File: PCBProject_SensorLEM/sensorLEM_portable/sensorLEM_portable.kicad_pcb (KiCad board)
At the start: 2 copper layers, 82 parts, among them CN1 DB2EVC-3.81-4P-GN, U1 VRB1212S-6WR3, U2 VRB1212S-6WR3, U3 FT-AX1D

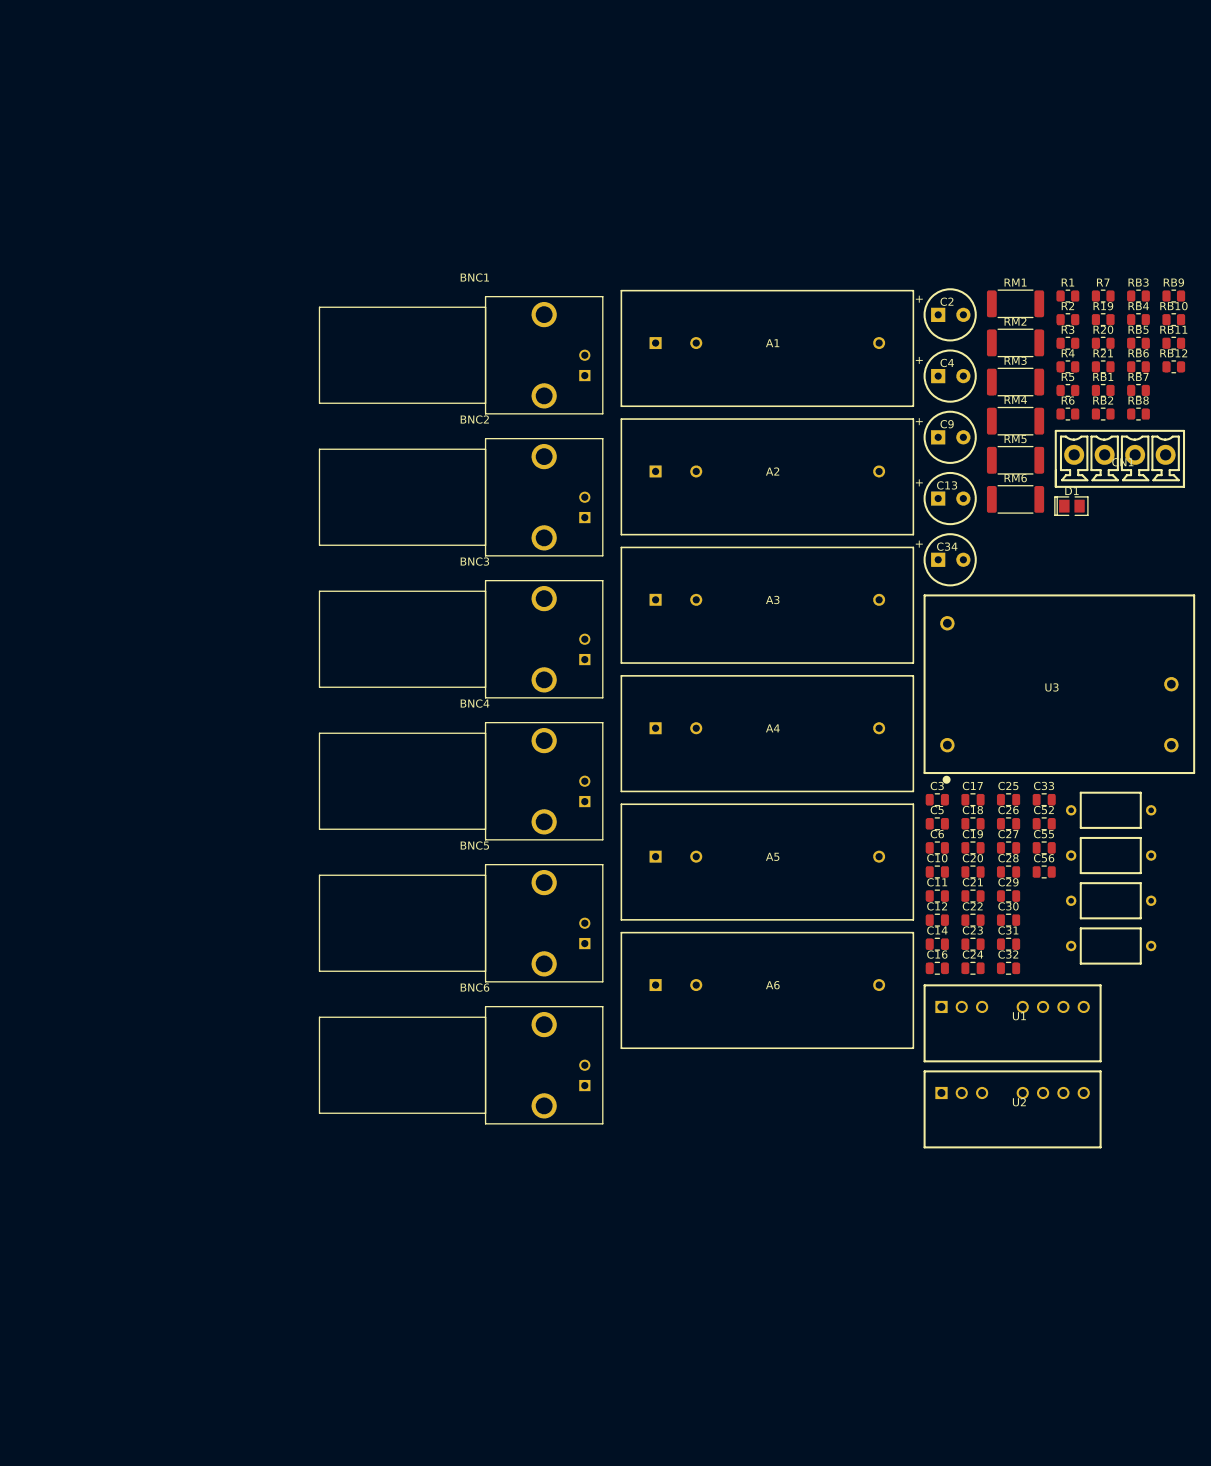
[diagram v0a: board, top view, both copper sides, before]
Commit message: sensorLEM_portable的原理图和Pcb都已经制作完毕，bom表和制作文件也都已经生成。
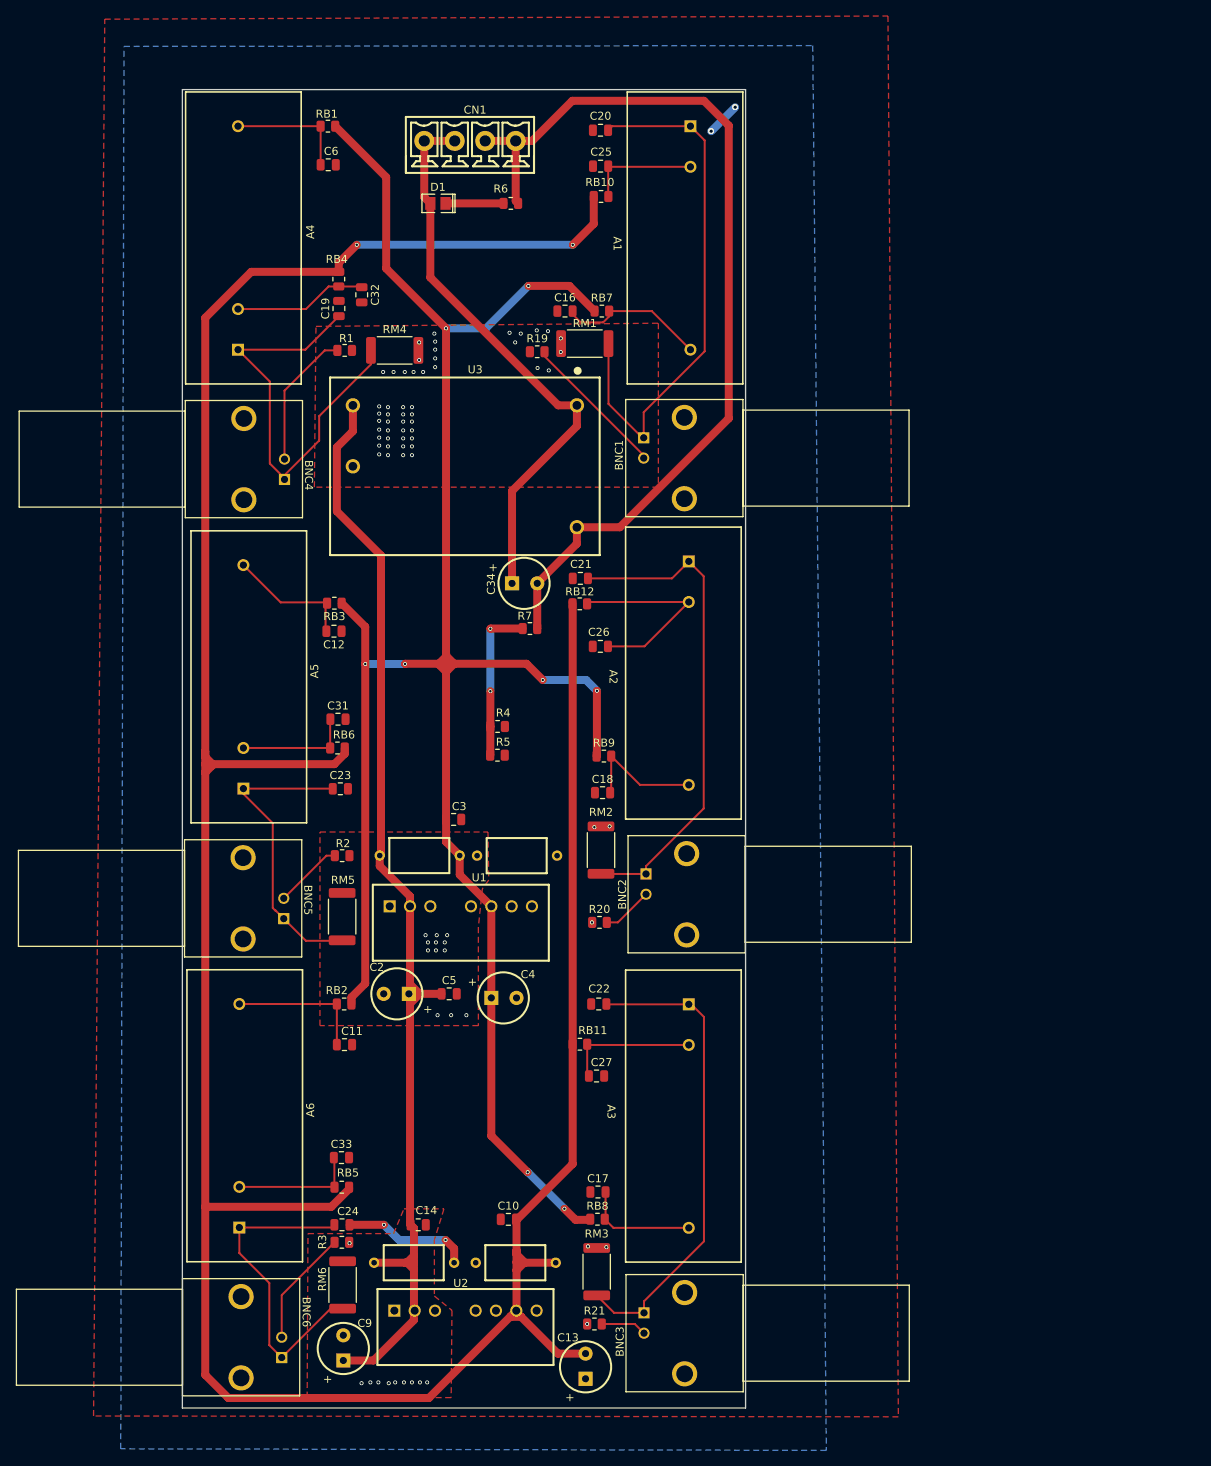
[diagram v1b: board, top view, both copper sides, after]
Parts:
- removed C28, C29, C30, C52, C55, C56: 102, Capacitor_SMD:C_0805_2012Metric
- moved RB5 145.1 mm to (87.2, 162.6)
- moved R3 144.5 mm to (87.2, 169.5), turned to 180 degrees
- moved C9 138.5 mm to (86.3, 183.1), turned to 90 degrees
- moved R21 135.5 mm to (118.8, 179.7)
- moved RM6 129.3 mm to (87.3, 174.8), turned to 90 degrees
- moved RM3 122.9 mm to (119.1, 173.2), turned to 90 degrees
- moved RB8 121.3 mm to (119.2, 166.6)
- moved RB2 120.2 mm to (87.5, 139.7), turned to 180 degrees
- moved C13 119.4 mm to (116.6, 185.4), turned to 90 degrees
- moved C32 116.7 mm to (89.7, 51.0), turned to -90 degrees
- moved RB11 114.8 mm to (117.0, 144.7), turned to 180 degrees
- moved C6 114.4 mm to (85.5, 34.8), turned to 180 degrees
- moved R2 112.8 mm to (87.3, 121.2), turned to 180 degrees
- moved RB6 110.9 mm to (86.7, 107.7)
- moved C2 110.7 mm to (94.5, 139.5), turned to 180 degrees
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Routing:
- net -12: track 0.00 -> 387.3 mm, vias 0 -> 2
- net +12: track 0.00 -> 270.1 mm, vias 0 -> 8
- net A12V: track 0.00 -> 145.9 mm
- net D12VGND: track 0.00 -> 117.7 mm
- net D12V1: track 0.00 -> 71.7 mm
- net /CSO1: track 0.00 -> 67.0 mm
- net /CSO2: track 0.00 -> 62.8 mm
- net /CSO3: track 0.00 -> 59.8 mm
- net /CSO4: track 0.00 -> 53.6 mm
- net /CSO6: track 0.00 -> 40.6 mm
- net /CSO5: track 0.00 -> 38.0 mm
- net Net-(A2-NEG): track 0.00 -> 25.6 mm
- net 12VGND: track 0.00 -> 20.3 mm, vias 0 -> 4
- net AGND: track 0.00 -> 19.9 mm, vias 0 -> 79
- net Net-(A1-POS): track 0.00 -> 18.5 mm
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- added copper zone on F.Cu, net 12VGND
- added copper zone on B.Cu, net AGND
- added copper zone on F.Cu, net AGND
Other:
- board outline added: 70.4 x 164.8 mm
